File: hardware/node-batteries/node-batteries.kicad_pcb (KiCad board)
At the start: 2 copper layers, 75 x 50 mm, 11 parts, among them J1 Conn_01x03_Male

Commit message: Added mounting tabs to battery PCB
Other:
- board size 75 x 50 mm -> 83 x 66 mm
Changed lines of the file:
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@@
   (general
     (thickness 1.6)
-    (drawings 45)
+    (drawings 96)
     (tracks 0)
     (zones 0)
@@
       (xy 0.0254 -0.041597)) (layer B.Cu) (width 0.01))
   )
+  (gr_line (start 41.5 100) (end 33.5 100) (layer Edge.Cuts) (width 0.15))
+  (gr_arc (start 48.5 106) (end 48.5 106.25) (angle -90) (layer Edge.Cuts) (width 0.15))
+  (gr_arc (start 48.5 103.25) (end 48.75 103.25) (angle -90) (layer Edge.Cuts) (width 0.15))
+  (gr_arc (start 41.5 99.75) (end 41.5 100) (angle -90) (layer Edge.Cuts) (width 0.15))
+  (gr_line (start 48.75 106) (end 48.75 103.25) (layer Edge.Cuts) (width 0.15))
+  (gr_line (start 43.75 108) (end 49.75 108) (layer Edge.Cuts) (width 0.15))
+  (gr_line (start 42.25 99.75) (end 42.25 106.5) (layer Edge.Cuts) (width 0.15))
+  (gr_line (start 44.75 103.25) (end 44.75 106) (layer Edge.Cuts) (width 0.15))
+  (gr_line (start 51.25 106.5) (end 51.25 99.75) (layer Edge.Cuts) (width 0.15))
+  (gr_arc (start 45 103.25) (end 45 103) (angle -90) (layer Edge.Cuts) (width 0.15))
+  (gr_line (start 48.5 103) (end 45 103) (layer Edge.Cuts) (width 0.15))
+  (gr_arc (start 45 106) (end 44.75 106) (angle -90) (layer Edge.Cuts) (width 0.15))
+  (gr_arc (start 49.75 106.5) (end 49.75 108) (angle -90) (layer Edge.Cuts) (width 0.15))
+  (gr_arc (start 52 99.75) (end 51.75 99.75) (angle -90) (layer Edge.Cuts) (width 0.15))
+  (gr_arc (start 43.75 106.5) (end 42.25 106.5) (angle -90) (layer Edge.Cuts) (width 0.15))
+  (gr_arc (start 51.5 99.75) (end 51.75 99.75) (angle -180) (layer Edge.Cuts) (width 0.15))
+  (gr_line (start 45 106.25) (end 48.5 106.25) (layer Edge.Cuts) (width 0.15))
+  (gr_arc (start 42 99.75) (end 42.25 99.75) (angle -180) (layer Edge.Cuts) (width 0.15))
+  (gr_line (start 41.5 50) (end 33.5 50) (layer Edge.Cuts) (width 0.15))
+  (gr_arc (start 45 44) (end 45 43.75) (angle -90) (layer Edge.Cuts) (width 0.15))
+  (gr_arc (start 45 46.75) (end 44.75 46.75) (angle -90) (layer Edge.Cuts) (width 0.15))
+  (gr_arc (start 52 50.25) (end 52 50) (angle -90) (layer Edge.Cuts) (width 0.15))
+  (gr_line (start 44.75 44) (end 44.75 46.75) (layer Edge.Cuts) (width 0.15))
+  (gr_line (start 49.75 42) (end 43.75 42) (layer Edge.Cuts) (width 0.15))
+  (gr_line (start 51.25 50.25) (end 51.25 43.5) (layer Edge.Cuts) (width 0.15))
+  (gr_line (start 48.75 46.75) (end 48.75 44) (layer Edge.Cuts) (width 0.15))
+  (gr_line (start 42.25 43.5) (end 42.25 50.25) (layer Edge.Cuts) (width 0.15))
+  (gr_arc (start 48.5 46.75) (end 48.5 47) (angle -90) (layer Edge.Cuts) (width 0.15))
+  (gr_line (start 45 47) (end 48.5 47) (layer Edge.Cuts) (width 0.15))
+  (gr_arc (start 48.5 44) (end 48.75 44) (angle -90) (layer Edge.Cuts) (width 0.15))
+  (gr_arc (start 43.75 43.5) (end 43.75 42) (angle -90) (layer Edge.Cuts) (width 0.15))
+  (gr_arc (start 41.5 50.25) (end 41.75 50.25) (angle -90) (layer Edge.Cuts) (width 0.15))
+  (gr_arc (start 49.75 43.5) (end 51.25 43.5) (angle -90) (layer Edge.Cuts) (width 0.15))
+  (gr_arc (start 42 50.25) (end 41.75 50.25) (angle -180) (layer Edge.Cuts) (width 0.15))
+  (gr_line (start 48.5 43.75) (end 45 43.75) (layer Edge.Cuts) (width 0.15))
+  (gr_arc (start 51.5 50.25) (end 51.25 50.25) (angle -180) (layer Edge.Cuts) (width 0.15))
+  (gr_arc (start 30.25 80.25) (end 30.25 80) (angle -90) (layer Edge.Cuts) (width 0.15))
+  (gr_arc (start 30.25 69.75) (end 30 69.75) (angle -90) (layer Edge.Cuts) (width 0.15))
+  (gr_arc (start 30.25 70.25) (end 30.25 70.5) (angle -180) (layer Edge.Cuts) (width 0.15))
+  (gr_arc (start 30.25 79.75) (end 30.25 80) (angle -180) (layer Edge.Cuts) (width 0.15))
+  (gr_arc (start 26.75 76.75) (end 26.75 77) (angle -90) (layer Edge.Cuts) (width 0.15))
+  (gr_arc (start 24 76.75) (end 23.75 76.75) (angle -90) (layer Edge.Cuts) (width 0.15))
+  (gr_arc (start 24 73.25) (end 24 73) (angle -90) (layer Edge.Cuts) (width 0.15))
+  (gr_arc (start 26.75 73.25) (end 27 73.25) (angle -90) (layer Edge.Cuts) (width 0.15))
+  (gr_arc (start 23.5 78) (end 22 78) (angle -90) (layer Edge.Cuts) (width 0.15))
+  (gr_arc (start 23.5 72) (end 23.5 70.5) (angle -90) (layer Edge.Cuts) (width 0.15))
+  (gr_line (start 30 53.5) (end 30 69.75) (layer Edge.Cuts) (width 0.15))
+  (gr_line (start 23.5 79.5) (end 30.25 79.5) (layer Edge.Cuts) (width 0.15))
+  (gr_line (start 22 72) (end 22 78) (layer Edge.Cuts) (width 0.15))
+  (gr_line (start 30.25 70.5) (end 23.5 70.5) (layer Edge.Cuts) (width 0.15))
+  (gr_line (start 27 76.75) (end 27 73.25) (layer Edge.Cuts) (width 0.15))
+  (gr_line (start 24 77) (end 26.75 77) (layer Edge.Cuts) (width 0.15))
+  (gr_line (start 23.75 73.25) (end 23.75 76.75) (layer Edge.Cuts) (width 0.15))
+  (gr_line (start 26.75 73) (end 24 73) (layer Edge.Cuts) (width 0.15))
   (dimension 48.5 (width 0.3) (layer Eco1.User)
     (gr_text "48,500 mm" (at 80.75 30.4) (layer Eco1.User)
@@
   (gr_circle (center 67.551216 75) (end 84 75) (layer F.SilkS) (width 0.5))
   (gr_line (start 67.5 50) (end 67.5 100) (layer Eco1.User) (width 0.2))
-  (gr_line (start 93.5 96) (end 93.5 98) (layer B.SilkS) (width 0.4))
   (gr_text V- (at 100 90.5) (layer B.SilkS)
     (effects (font (size 1.25 1.25) (thickness 0.3)) (justify left mirror))
@@
     (effects (font (size 1.25 1.25) (thickness 0.3)) (justify right))
   )
-  (gr_circle (center 41.5 97) (end 43.5 97) (layer B.SilkS) (width 0.4))
-  (gr_line (start 40.5 97) (end 42.5 97) (layer B.SilkS) (width 0.4))
-  (gr_circle (center 93.5 97) (end 95.5 97) (layer B.SilkS) (width 0.4))
-  (gr_line (start 92.5 97) (end 94.5 97) (layer B.SilkS) (width 0.4))
-  (gr_line (start 40.5 53) (end 42.5 53) (layer B.SilkS) (width 0.4))
-  (gr_line (start 41.5 52) (end 41.5 54) (layer B.SilkS) (width 0.4))
-  (gr_circle (center 41.5 53) (end 43.5 53) (layer B.SilkS) (width 0.4))
-  (gr_line (start 92.5 53) (end 94.5 53) (layer B.SilkS) (width 0.4))
-  (gr_circle (center 93.5 53) (end 95.5 53) (layer B.SilkS) (width 0.4))
+  (gr_circle (center 34.25 84.5) (end 36.25 84.5) (layer B.SilkS) (width 0.4))
+  (gr_line (start 33.25 84.5) (end 35.25 84.5) (layer B.SilkS) (width 0.4))
+  (gr_line (start 33.25 65.75) (end 35.25 65.75) (layer B.SilkS) (width 0.4))
+  (gr_line (start 34.25 64.75) (end 34.25 66.75) (layer B.SilkS) (width 0.4))
+  (gr_circle (center 34.25 65.75) (end 36.25 65.75) (layer B.SilkS) (width 0.4))
+  (gr_line (start 99.75 65.75) (end 101.75 65.75) (layer B.SilkS) (width 0.4))
+  (gr_circle (center 100.75 65.75) (end 102.75 65.75) (layer B.SilkS) (width 0.4))
   (gr_circle (center 33.5 96.5) (end 35.5 96.5) (layer F.SilkS) (width 0.2))
   (gr_circle (center 33.5 53.5) (end 35.5 53.5) (layer F.SilkS) (width 0.2))
@@
   (gr_arc (start 101.5 53.5) (end 105 53.5) (angle -90) (layer Edge.Cuts) (width 0.15))
   (gr_line (start 105 53.5) (end 105 96.5) (layer Edge.Cuts) (width 0.15))
-  (gr_line (start 33.5 50) (end 101.5 50) (layer Edge.Cuts) (width 0.15))
-  (gr_line (start 33.5 100) (end 101.5 100) (layer Edge.Cuts) (width 0.15))
-  (gr_line (start 30 53.5) (end 30 96.5) (layer Edge.Cuts) (width 0.15))
+  (gr_line (start 52 50) (end 101.5 50) (layer Edge.Cuts) (width 0.15))
+  (gr_line (start 52 100) (end 101.5 100) (layer Edge.Cuts) (width 0.15))
+  (gr_line (start 30 80.25) (end 30 96.5) (layer Edge.Cuts) (width 0.15))
   (gr_arc (start 33.5 53.5) (end 33.5 50) (angle -90) (layer Edge.Cuts) (width 0.15))
   (gr_arc (start 33.5 96.5) (end 30 96.5) (angle -90) (layer Edge.Cuts) (width 0.15))
@@
     (connect_pads (clearance 0.508))
     (min_thickness 0.254)
-    (fill yes (arc_segments 16) (thermal_gap 0.508) (thermal_bridge_width 0.508))
+    (fill yes (arc_segments 16) (thermal_gap 0.508) (thermal_bridge_width 0.508) (smoothing chamfer) (radius 1))
     (polygon
       (pts
-        (xy 25 45) (xy 110 45) (xy 110 105) (xy 25 105)
+        (xy 25 45) (xy 110 45) (xy 110 105) (xy 74 105) (xy 74 90)
+        (xy 58 90) (xy 58 105) (xy 25 105)
       )
     )
@@
       (pts
         (xy 107 87) (xy 87 87) (xy 87 47) (xy 26 47) (xy 26 102)
-        (xy 107 102)
+        (xy 58 102) (xy 58 90) (xy 74 90) (xy 74 102) (xy 107 102)
       )
     )

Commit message: Layout improvemnets
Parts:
- MH1, MH2, MH3, MH4, MH6: footprint MountingHole:MountingHole_3.2mm_M3 -> MountingHole:MountingHole_3.2mm_M3_Pad
- MH5: footprint MountingHole:MountingHole_3.2mm_M3 -> humidity:MountingHole_3.2mm_M3
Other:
- board text added: "OOS 2019-06-17"
- board text removed: "2019-06-03"

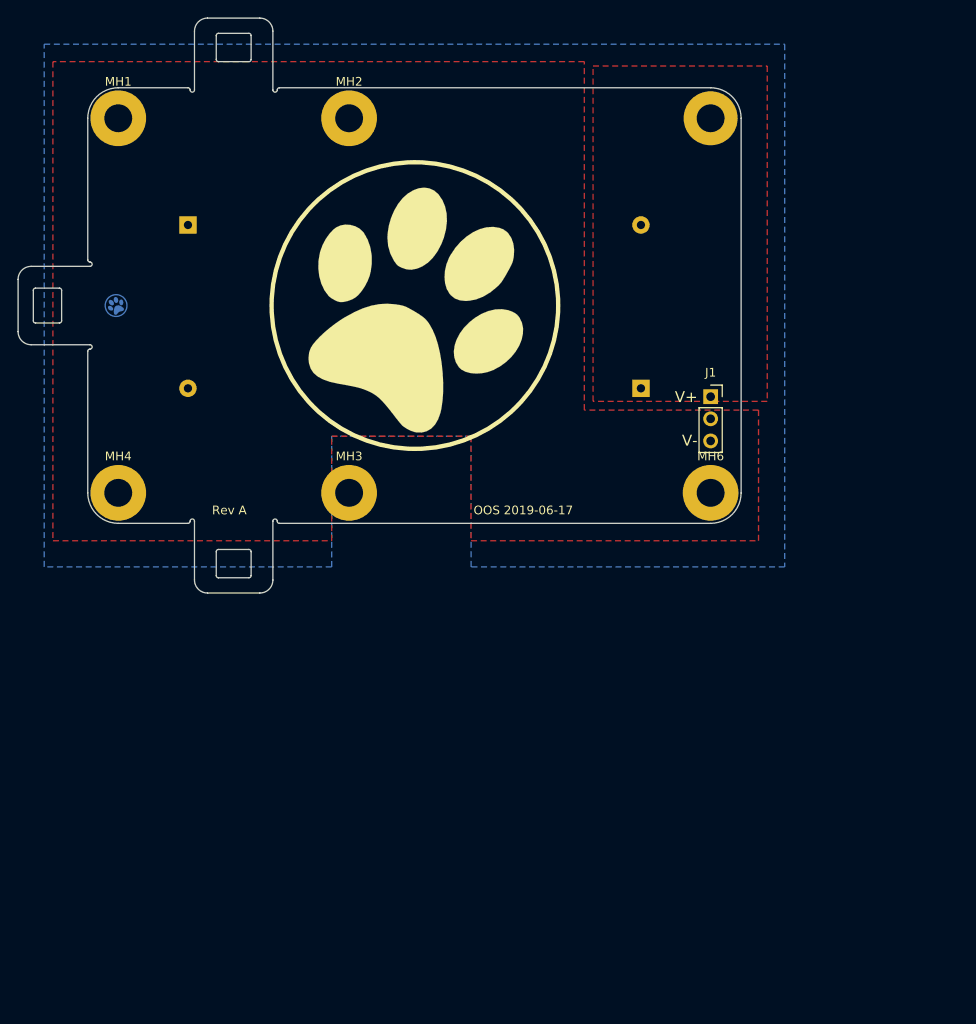
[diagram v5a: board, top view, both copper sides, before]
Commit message: Improved mounting holes and planes
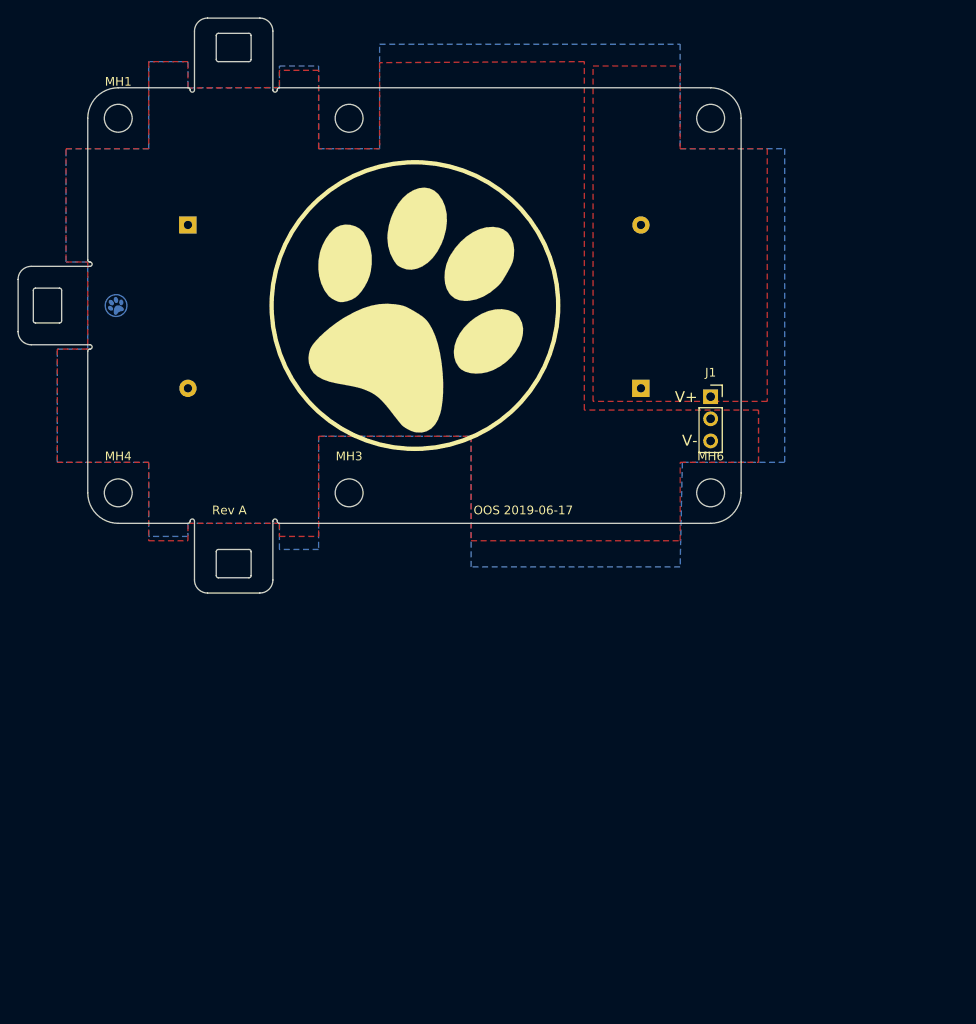
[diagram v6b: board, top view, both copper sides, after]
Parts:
- MH1, MH2, MH3, MH4, MH6: footprint MountingHole:MountingHole_3.2mm_M3_Pad -> humidity:MountingHole_3.2mm_M3

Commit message: Minor layout adjustments
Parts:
- moved G*** 0.25 mm to (33.5, 75.0)
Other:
- board text added: "OOS 2019-06-22"
- board text removed: "OOS 2019-06-17"
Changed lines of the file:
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@@
     (tags "mounting hole 3.2mm no annular m3")
     (attr virtual)
-    (fp_text reference MH1 (at 0 -4.2) (layer F.SilkS)
+    (fp_text reference MH1 (at 0 -4.2) (layer F.SilkS) hide
       (effects (font (size 1 1) (thickness 0.15)))
     )
@@
     (tags "mounting hole 3.2mm no annular m3")
     (attr virtual)
-    (fp_text reference MH3 (at 0 -4.2) (layer F.SilkS)
+    (fp_text reference MH3 (at 0 -4.2) (layer F.SilkS) hide
       (effects (font (size 1 1) (thickness 0.15)))
     )
@@
     (tags "mounting hole 3.2mm no annular m3")
     (attr virtual)
-    (fp_text reference MH4 (at 0 -4.2) (layer F.SilkS)
+    (fp_text reference MH4 (at 0 -4.2) (layer F.SilkS) hide
       (effects (font (size 1 1) (thickness 0.15)))
     )
@@
     (tags "mounting hole 3.2mm no annular m3")
     (attr virtual)
-    (fp_text reference MH6 (at 0 -4.2) (layer F.SilkS)
+    (fp_text reference MH6 (at 0 -4.2) (layer F.SilkS) hide
       (effects (font (size 1 1) (thickness 0.15)))
     )
@@
   )
   (module humidity:paw-cu-circ (layer B.Cu)
-    (at 33.25 75 210)
+    (at 33.5 75 210)
     (fp_text reference G*** (at 0 0 210) (layer B.SilkS) hide
       (effects (font (size 1.524 1.524) (thickness 0.3)) (justify mirror))
@@
     (arrow2b (pts (xy 105 32.5) (xy 103.873496 33.086421)))
   )
-  (gr_text "OOS 2019-06-17" (at 80 98.5) (layer F.SilkS)
+  (gr_text "OOS 2019-06-22" (at 86 98.5) (layer F.SilkS)
     (effects (font (size 1 1) (thickness 0.2)))
   )
@@
     (effects (font (size 1.25 1.25) (thickness 0.3)) (justify right))
   )
-  (gr_circle (center 34.25 84.5) (end 36.25 84.5) (layer B.SilkS) (width 0.4))
-  (gr_line (start 33.25 84.5) (end 35.25 84.5) (layer B.SilkS) (width 0.4))
-  (gr_line (start 33.25 65.75) (end 35.25 65.75) (layer B.SilkS) (width 0.4))
-  (gr_line (start 34.25 64.75) (end 34.25 66.75) (layer B.SilkS) (width 0.4))
-  (gr_circle (center 34.25 65.75) (end 36.25 65.75) (layer B.SilkS) (width 0.4))
-  (gr_line (start 99.75 65.75) (end 101.75 65.75) (layer B.SilkS) (width 0.4))
-  (gr_circle (center 100.75 65.75) (end 102.75 65.75) (layer B.SilkS) (width 0.4))
+  (gr_circle (center 33.5 84.5) (end 35.5 84.5) (layer B.SilkS) (width 0.4))
+  (gr_line (start 32.5 84.5) (end 34.5 84.5) (layer B.SilkS) (width 0.4))
+  (gr_line (start 32.5 65.75) (end 34.5 65.75) (layer B.SilkS) (width 0.4))
+  (gr_line (start 33.5 64.75) (end 33.5 66.75) (layer B.SilkS) (width 0.4))
+  (gr_circle (center 33.5 65.75) (end 35.5 65.75) (layer B.SilkS) (width 0.4))
+  (gr_line (start 100.5 65.75) (end 102.5 65.75) (layer B.SilkS) (width 0.4))
+  (gr_circle (center 101.5 65.75) (end 103.5 65.75) (layer B.SilkS) (width 0.4))
   (gr_line (start 105.5 75) (end 30 75) (layer Eco1.User) (width 0.15))
   (gr_arc (start 101.5 96.5) (end 101.5 100) (angle -90) (layer Edge.Cuts) (width 0.15))
